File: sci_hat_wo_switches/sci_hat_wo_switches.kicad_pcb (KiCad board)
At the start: 4 copper layers, 36.2 x 80 mm, 54 parts, among them J1 10051922-2410EHLF, J2 10051922-2410EHLF, J3 10051922-2410EHLF, J4 Conn_02x11_Odd_Even, J5 Conn_02x07_Odd_Even, U1 TPS22968QDMGRQ1, U2 TPS22968QDMGRQ1, U3 TPS22968QDMGRQ1, U4 TCA9546APWR

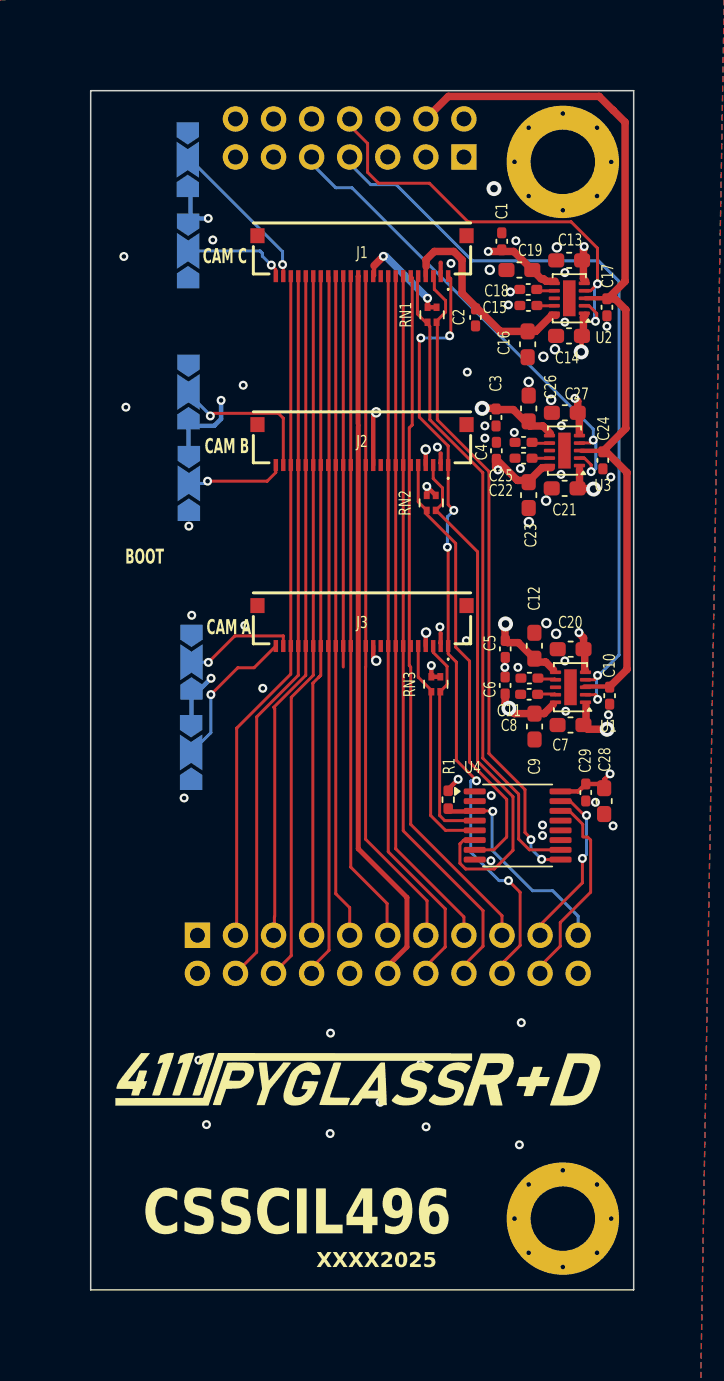
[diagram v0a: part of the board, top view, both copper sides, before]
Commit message: switchless hat roughed in
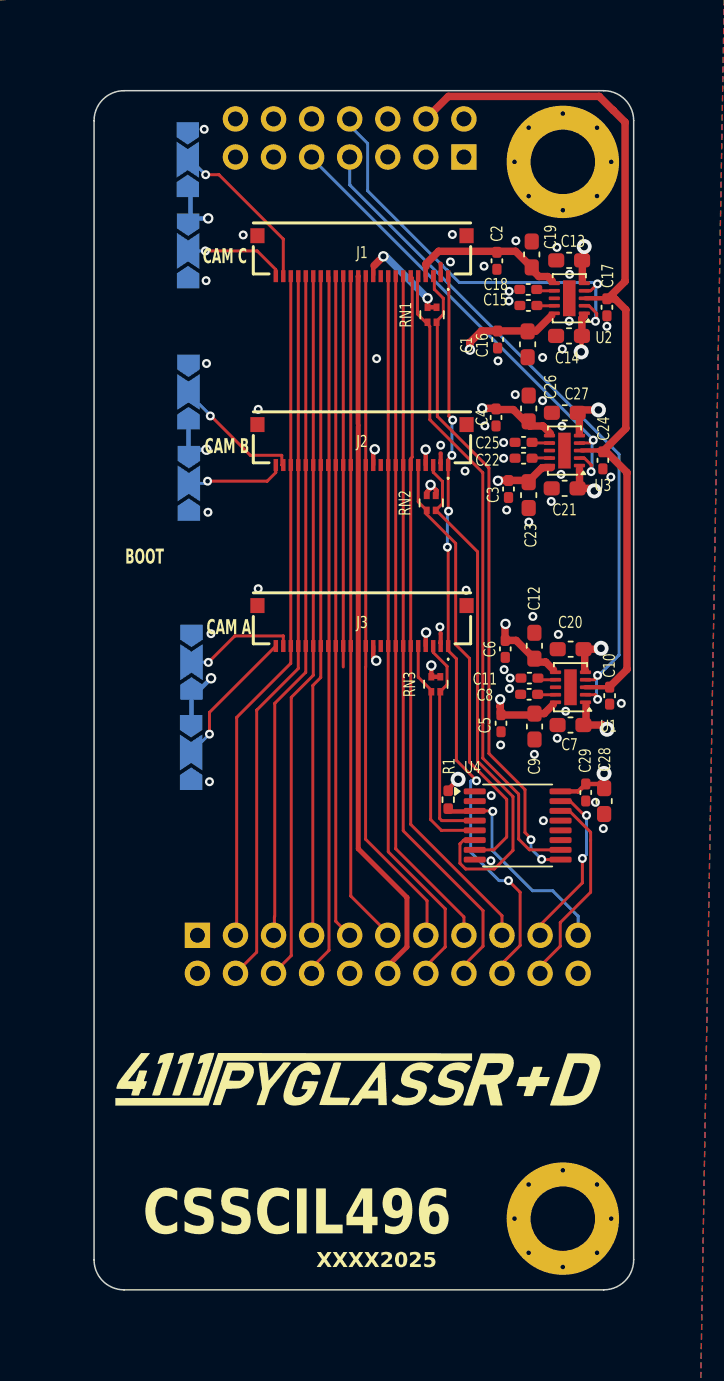
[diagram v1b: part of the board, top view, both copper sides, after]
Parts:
- moved C1 6.56 mm to (130.9, 76.6), turned to -90 degrees
- moved C5 4.97 mm to (131.1, 102.2)
- moved C3 4.85 mm to (131.6, 86.6)
- moved C2 4.04 mm to (130.8, 71.3)
- moved C6 2.44 mm to (131.4, 97.2), turned to -90 degrees
- moved C4 2.23 mm to (130.8, 81.8), turned to -90 degrees
- moved C19 1.32 mm to (133.2, 70.9), turned to -90 degrees
- moved NT1 0.08 mm to (127.1, 71.9)
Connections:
- C12 pad 2: /CameraHat/1V8_A -> /CameraHat/2V8_A
- C13 pad 1: +1V8 -> +2V8
- C14 pad 1: +2V8 -> +1V8
- C16 pad 1: /CameraHat/2V8_C -> /CameraHat/1V8_C
- C19 pad 2: /CameraHat/1V8_C -> /CameraHat/2V8_C
- C20 pad 1: +1V8 -> +2V8
- C21 pad 1: +2V8 -> +1V8
- C23 pad 1: /CameraHat/2V8_B -> /CameraHat/1V8_B
- C26 pad 2: /CameraHat/1V8_B -> /CameraHat/2V8_B
- C27 pad 1: +1V8 -> +2V8
- C7 pad 1: +2V8 -> +1V8
- C9 pad 1: /CameraHat/2V8_A -> /CameraHat/1V8_A
- U1 pad 1: +2V8 -> +1V8
- U1 pad 10: /CameraHat/2V8_A -> /CameraHat/1V8_A
- U1 pad 5: +1V8 -> +2V8
- U1 pad 6: /CameraHat/1V8_A -> /CameraHat/2V8_A
- U2 pad 1: +2V8 -> +1V8
- U2 pad 10: /CameraHat/2V8_C -> /CameraHat/1V8_C
- U2 pad 5: +1V8 -> +2V8
- U2 pad 6: /CameraHat/1V8_C -> /CameraHat/2V8_C
- U3 pad 1: +2V8 -> +1V8
- U3 pad 10: /CameraHat/2V8_B -> /CameraHat/1V8_B
- U3 pad 5: +1V8 -> +2V8
- U3 pad 6: /CameraHat/1V8_B -> /CameraHat/2V8_B
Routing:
- net +2V8: track 63.9 -> 50.8 mm
- net /CameraHat/1V8_B: track 40.3 -> 30.4 mm
- net /CameraHat/2V8_A: track 21.5 -> 12.1 mm
- net +1V8: track 80.4 -> 71.8 mm
- net /CameraHat/2V8_B: track 19.7 -> 12.2 mm
- net /CameraHat/ENABLE_A: track 51.8 -> 45.9 mm
- net /CameraHat/2V8_C: track 14.0 -> 10.4 mm
- net /CameraHat/STROBE: track 52.3 -> 49.5 mm
- net /CameraHat/1V8_C: track 35.7 -> 37.6 mm
- net /CameraHat/1V8_A: track 33.1 -> 31.2 mm
- net Net-(JP3-C): track 10.3 -> 8.48 mm
- net /CameraHat/ENABLE_B: track 31.7 -> 30.8 mm
- net /CameraHat/ENABLE_C: track 28.6 -> 27.8 mm
- net Net-(JP6-C): track 10.1 -> 9.44 mm
- net Net-(JP1-C): track 10.3 -> 10.9 mm
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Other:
- board size 36.2 x 80 mm -> 36 x 80 mm

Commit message: move camera connector to common
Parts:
- removed J4: Conn_02x11_Odd_Even, Connector_PinHeader_2.54mm:PinHeader_2x11_P2.54mm_Vertical
- removed J5: Conn_02x07_Odd_Even, Connector_PinHeader_2.54mm:PinHeader_2x07_P2.54mm_Vertical
- added J10: Conn_02x11_Odd_Even, Connector_PinHeader_2.54mm:PinHeader_2x11_P2.54mm_Vertical, B.Cu at (110.9, 116.3)
- added J11: Conn_02x07_Odd_Even, Connector_PinHeader_2.54mm:PinHeader_2x07_P2.54mm_Vertical, B.Cu at (128.7, 64.4)
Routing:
- net /CameraHat/I2C_SDA: track 10.7 -> 12.0 mm, vias 2 -> 0
- net (no net): track 0.80 -> 0.00 mm
- net /CameraHat/I2C_RST: track 14.2 -> 13.4 mm
- net /CameraHat/I2C_SCK: track 12.4 -> 12.1 mm, vias 0 -> 2
